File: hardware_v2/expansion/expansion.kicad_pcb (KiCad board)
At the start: 2 copper layers, 13 parts, among them J2 Conn_02x10_Odd_Even

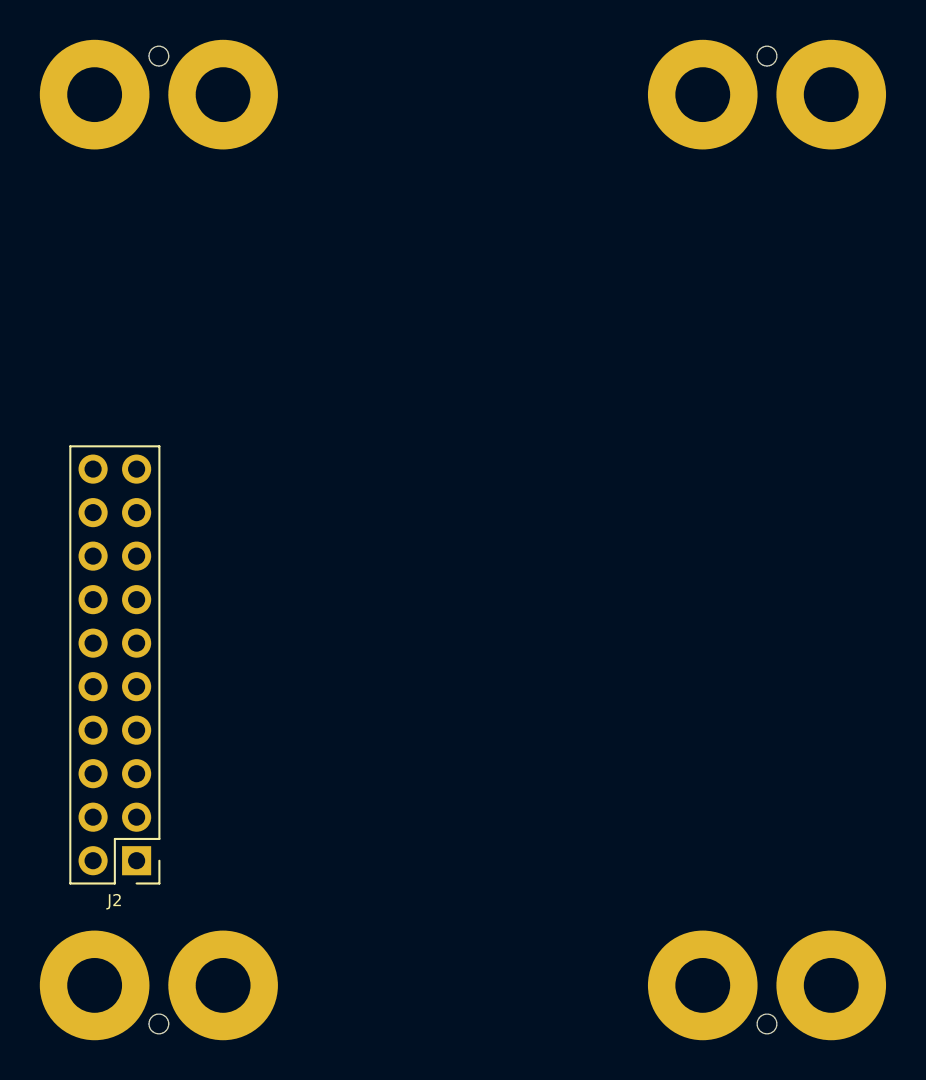
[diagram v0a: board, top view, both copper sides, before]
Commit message: PCB: Add draft of expansion board outline
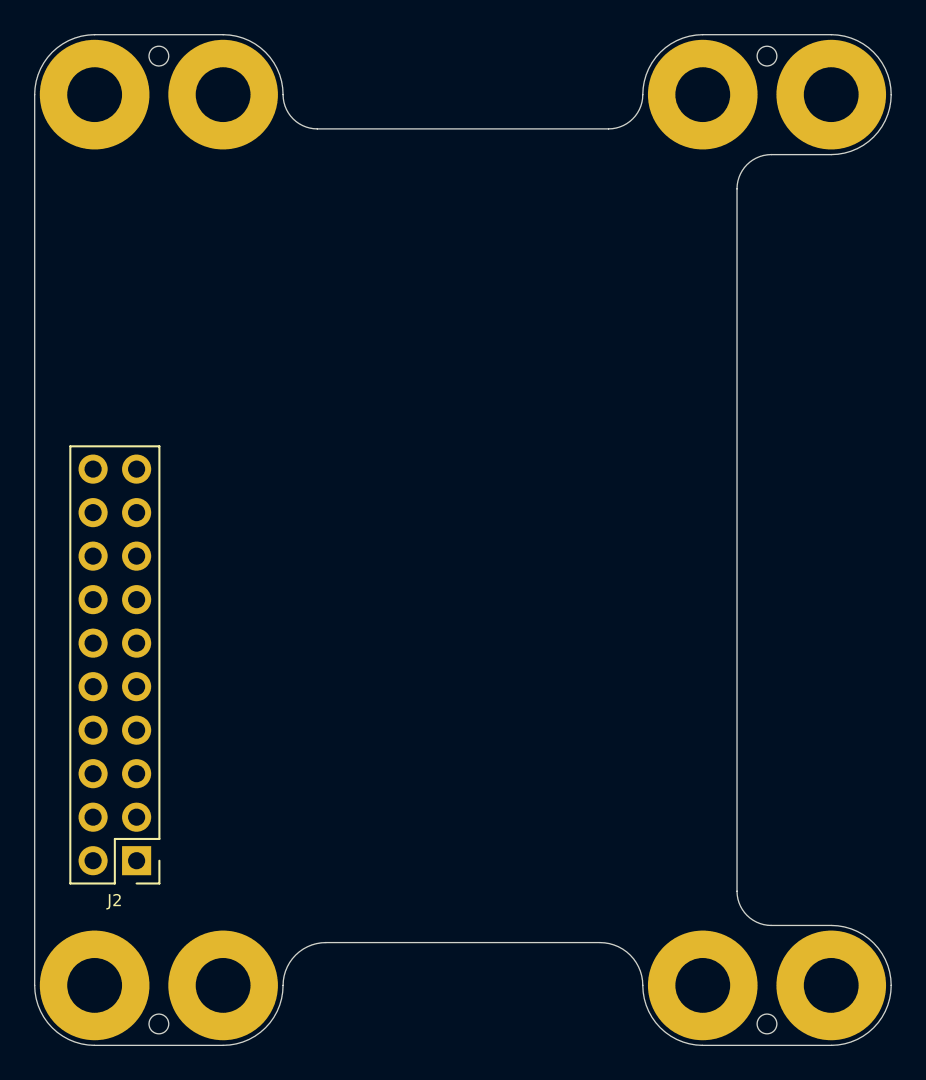
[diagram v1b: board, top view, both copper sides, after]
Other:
- board outline added: 50 x 59 mm
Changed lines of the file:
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@@
   (setup
     (pad_to_mask_clearance 0)
+    (grid_origin 125 60)
     (pcbplotparams
       (layerselection 0x00010fc_ffffffff)
@@
       (net 1 "GND") (pinfunction "1") (pintype "input"))
   )
+  (gr_arc (start 116.5 63) (mid 115.085786 62.414214) (end 114.5 61)
+    (stroke (width 0.05) (type default)) (layer "Edge.Cuts"))
+  (gr_arc (start 111 57.5) (mid 113.474874 58.525126) (end 114.5 61)
+    (stroke (width 0.05) (type default)) (layer "Edge.Cuts"))
+  (gr_line (start 100 61) (end 100 113)
+    (stroke (width 0.05) (type default)) (layer "Edge.Cuts"))
+  (gr_line (start 146.5 57.5) (end 139 57.5)
+    (stroke (width 0.05) (type default)) (layer "Edge.Cuts"))
+  (gr_arc (start 150 61) (mid 148.974874 63.474874) (end 146.5 64.5)
+    (stroke (width 0.05) (type default)) (layer "Edge.Cuts"))
+  (gr_arc (start 114.5 113) (mid 113.474874 115.474874) (end 111 116.5)
+    (stroke (width 0.05) (type default)) (layer "Edge.Cuts"))
+  (gr_arc (start 139 116.5) (mid 136.525126 115.474874) (end 135.5 113)
+    (stroke (width 0.05) (type default)) (layer "Edge.Cuts"))
+  (gr_line (start 103.5 57.5) (end 111 57.5)
+    (stroke (width 0.05) (type default)) (layer "Edge.Cuts"))
+  (gr_line (start 133 110.5) (end 117 110.5)
+    (stroke (width 0.05) (type default)) (layer "Edge.Cuts"))
+  (gr_arc (start 143 109.5) (mid 141.585786 108.914214) (end 141 107.5)
+    (stroke (width 0.05) (type default)) (layer "Edge.Cuts"))
+  (gr_line (start 141 107.5) (end 141 66.5)
+    (stroke (width 0.05) (type default)) (layer "Edge.Cuts"))
+  (gr_arc (start 141 66.5) (mid 141.585786 65.085786) (end 143 64.5)
+    (stroke (width 0.05) (type default)) (layer "Edge.Cuts"))
+  (gr_line (start 143 109.5) (end 146.5 109.5)
+    (stroke (width 0.05) (type default)) (layer "Edge.Cuts"))
+  (gr_arc (start 100 61) (mid 101.025126 58.525126) (end 103.5 57.5)
+    (stroke (width 0.05) (type default)) (layer "Edge.Cuts"))
+  (gr_line (start 116.5 63) (end 133.5 63)
+    (stroke (width 0.05) (type default)) (layer "Edge.Cuts"))
+  (gr_arc (start 146.5 57.5) (mid 148.974874 58.525126) (end 150 61)
+    (stroke (width 0.05) (type default)) (layer "Edge.Cuts"))
+  (gr_arc (start 114.5 113) (mid 115.232233 111.232233) (end 117 110.5)
+    (stroke (width 0.05) (type default)) (layer "Edge.Cuts"))
+  (gr_arc (start 150 113) (mid 148.974874 115.474874) (end 146.5 116.5)
+    (stroke (width 0.05) (type default)) (layer "Edge.Cuts"))
+  (gr_line (start 139 116.5) (end 146.5 116.5)
+    (stroke (width 0.05) (type default)) (layer "Edge.Cuts"))
+  (gr_arc (start 103.5 116.5) (mid 101.025126 115.474874) (end 100 113)
+    (stroke (width 0.05) (type default)) (layer "Edge.Cuts"))
+  (gr_line (start 103.5 116.5) (end 111 116.5)
+    (stroke (width 0.05) (type default)) (layer "Edge.Cuts"))
+  (gr_arc (start 135.5 61) (mid 134.914214 62.414214) (end 133.5 63)
+    (stroke (width 0.05) (type default)) (layer "Edge.Cuts"))
+  (gr_arc (start 146.5 109.5) (mid 148.974874 110.525126) (end 150 113)
+    (stroke (width 0.05) (type default)) (layer "Edge.Cuts"))
+  (gr_line (start 146.5 64.5) (end 143 64.5)
+    (stroke (width 0.05) (type default)) (layer "Edge.Cuts"))
+  (gr_arc (start 133 110.5) (mid 134.767767 111.232233) (end 135.5 113)
+    (stroke (width 0.05) (type default)) (layer "Edge.Cuts"))
+  (gr_arc (start 135.5 61) (mid 136.525126 58.525126) (end 139 57.5)
+    (stroke (width 0.05) (type default)) (layer "Edge.Cuts"))
 )
